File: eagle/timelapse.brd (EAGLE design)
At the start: 48.3 x 47 mm, 21 parts, among them Q1 200mA/40V, Q2 60V/32A/35mΩ, U2 TSR_1-2450

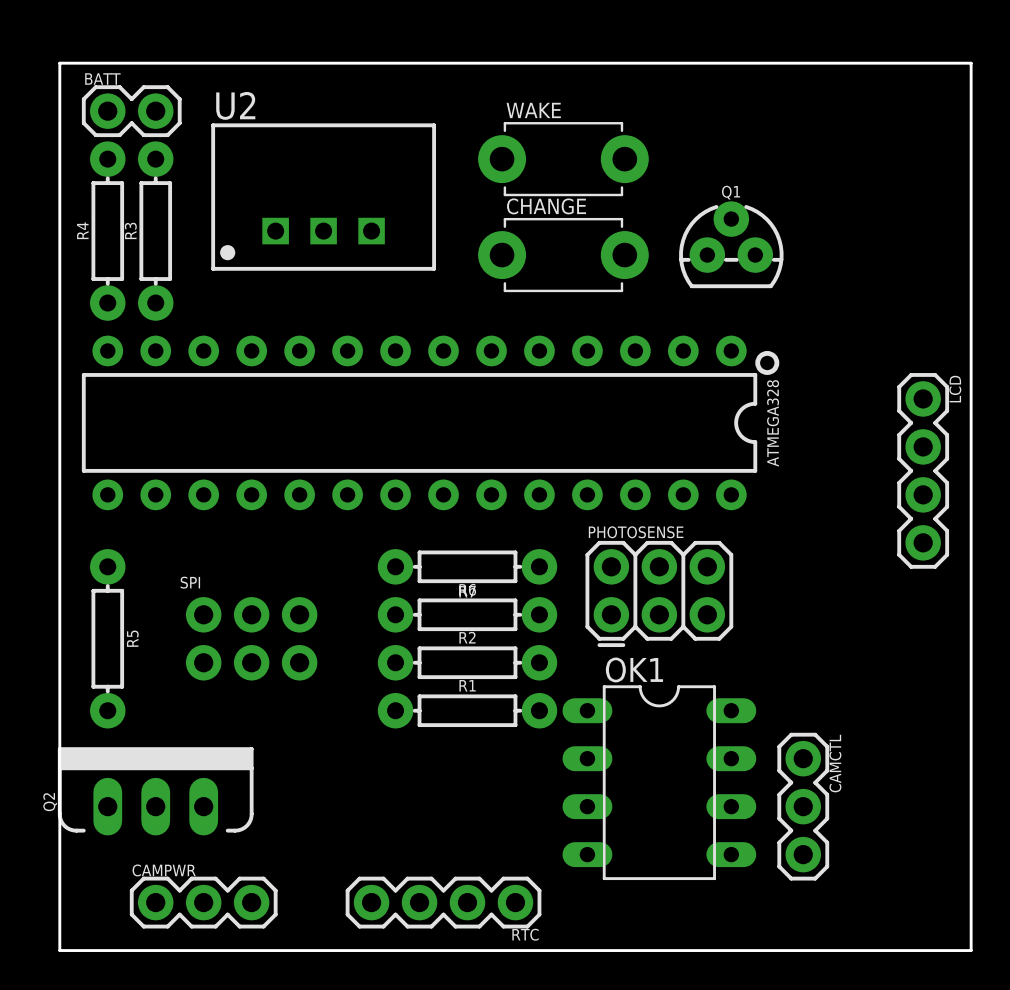
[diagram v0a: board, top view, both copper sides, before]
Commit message: Remove old EAGLE files, fix missing wires in schema and add test points.
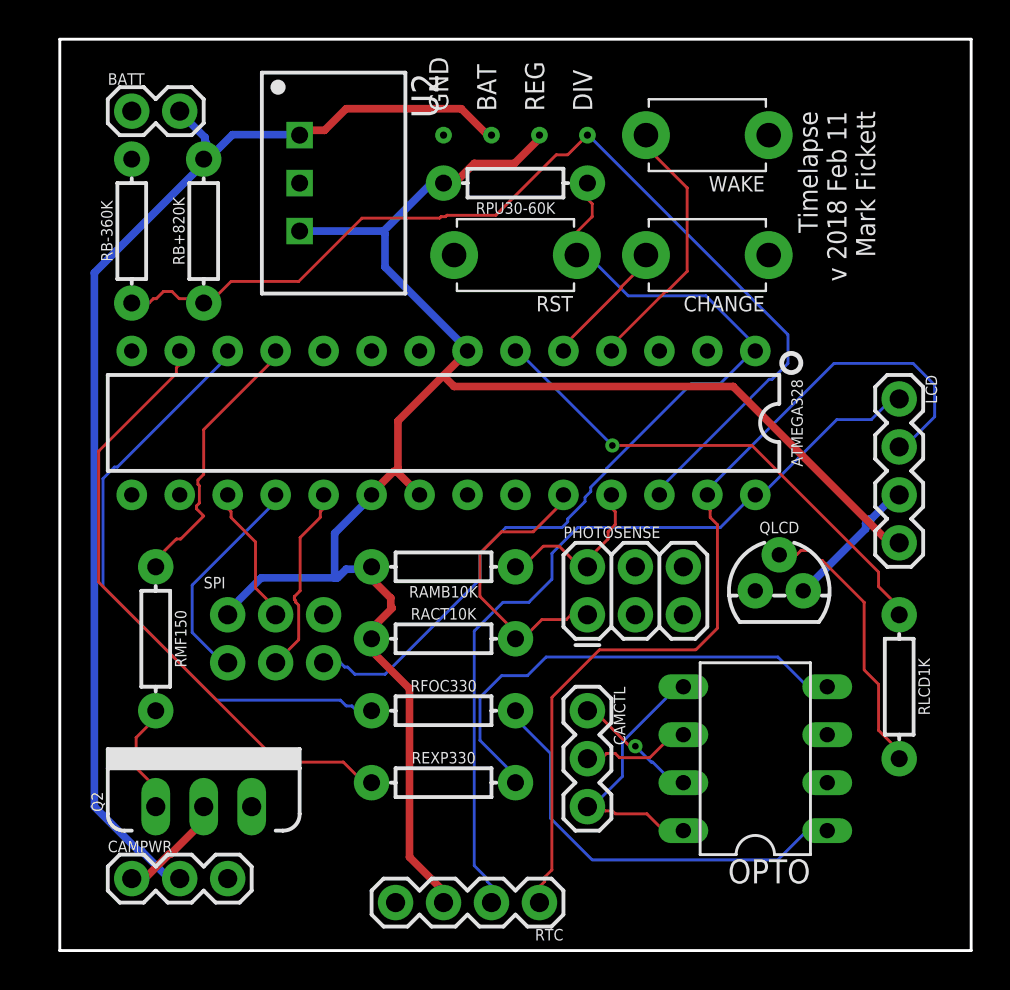
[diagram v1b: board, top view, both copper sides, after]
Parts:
- removed OK1: ILD2, optocoupler-2:DIL08
- removed Q1: 200mA/40V, SparkFun-DiscreteSemi:TO-92
- removed R1, R2, R5: 330, SparkFun-Resistors:AXIAL-0.3
- removed R3, R4, R6, R7: 10k, SparkFun-Resistors:AXIAL-0.3
- added OPTO: ILD2, optocoupler-2:DIL08
- added QLCD: 200mA/40V, SparkFun-DiscreteSemi:TO-92
- added RACT10K, RAMB10K: 10k, SparkFun-Resistors:AXIAL-0.3
- added RB+820K: 820k, SparkFun-Resistors:AXIAL-0.3
- added RB-360K: 360k, SparkFun-Resistors:AXIAL-0.3
- added REXP330, RFOC330: 330, SparkFun-Resistors:AXIAL-0.3
- added RLCD1K: 1k, SparkFun-Resistors:AXIAL-0.3
- added RMF150: 150, SparkFun-Resistors:AXIAL-0.3
- added RPU30-60K: 30-60k, SparkFun-Resistors:AXIAL-0.3
- added RST: (no value), adafruit:TACT_PANA-EVQ
- added TPBATT, TPDIV, TPGND, TPVREG: TEST-POINTTP_15TH_THRU, SparkFun-Connectors:TP_15TH
- moved CAMCTL 11.7 mm to (27.9, 12.7)
- moved WAKE 7.73 mm to (34.3, 43.2), turned to 180 degrees
- moved CHANGE 7.62 mm to (34.3, 36.8), turned to 180 degrees
- moved U2 2.84 mm to (12.7, 40.6), turned to 270 degrees
- moved Q2 2.54 mm to (7.62, 7.62)
- moved CAMPWR 1.80 mm to (3.81, 3.81)
- moved BATT 1.27 mm to (3.81, 44.5)
- moved ATMEGA328 1.27 mm to (20.3, 27.9)
- moved PHOTOSENSE 1.27 mm to (27.9, 17.8)
- moved RTC 1.27 mm to (25.4, 2.54)
- moved SPI 1.27 mm to (11.4, 16.5)
- moved LCD 1.27 mm to (44.5, 29.2)
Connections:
- removed net 3.3V: ATMEGA328.22, ATMEGA328.8, BATT.1, CHANGE.P$1, OK1.2, OK1.3, PHOTOSENSE.3, PHOTOSENSE.4, Q1.1, Q2.3, R4.P$2, RTC.4, SPI.6, U2.2, WAKE.P$1
- removed net N$4: ATMEGA328.12, R2.P$1
- removed net VCC2: BATT.2, CAMPWR.2, R3.P$2, U2.1
- new net BATVCC: BATT.2, CAMPWR.2, RB+820K.P$2, TPBATT.P$1, U2.1
- new net CAMGND: CAMCTL.3, OPTO.5, OPTO.8
- new net D6: ATMEGA328.12, RFOC330.P$1
- new net D7: ATMEGA328.13, REXP330.P$1
- new net RST: ATMEGA328.1, RPU30-60K.P$1, RST.P$1, SPI.5
- net ACTSENSE: now also RACT10K.P$2; no longer R6.P$2
- net AMBSENSE: now also RAMB10K.P$1; no longer R7.P$1
- net BATTSENSE: now also RB+820K.P$1, RB-360K.P$1, TPDIV.P$1; no longer R3.P$1, R4.P$1
- net D4: now also RLCD1K.P$1; no longer Q1.2
- net D5: now also RMF150.P$1; no longer R5.P$1
- net EXPOSE: now also OPTO.6; no longer OK1.6
- net FOCUS: now also OPTO.7; no longer OK1.7
- net GND: now also ATMEGA328.22, ATMEGA328.8, BATT.1, CHANGE.P$1, OPTO.2, OPTO.3, PHOTOSENSE.5, PHOTOSENSE.6, Q2.3, QLCD.1, RB-360K.P$2, RST.P$2, RTC.4, SPI.6, TPGND.P$1, U2.2, WAKE.P$1; no longer CAMCTL.3, OK1.5, OK1.8
- net N$1: now also OPTO.1, RFOC330.P$2; no longer OK1.1, R2.P$2
- net N$2: now also OPTO.4, REXP330.P$2; no longer OK1.4, R1.P$2
- net N$3: now also QLCD.2, RLCD1K.P$2; no longer ATMEGA328.13, R1.P$1
- net N$5: now also QLCD.3; no longer Q1.3
- net N$6: now also RMF150.P$2; no longer R5.P$2
- net VCCA: now also ATMEGA328.20, ATMEGA328.21, RACT10K.P$1, RAMB10K.P$2, RPU30-60K.P$2, TPVREG.P$1; no longer R6.P$1, R7.P$2
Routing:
- net VCCA: track 0.00 -> 96.7 mm
- net BATVCC: track 0.00 -> 63.0 mm
- net BATTSENSE: track 0.00 -> 54.7 mm
- net SDA: track 0.00 -> 48.5 mm
- net RST: track 0.00 -> 47.6 mm
- net SCL: track 0.00 -> 43.2 mm
- net D7: track 0.00 -> 32.9 mm
- net D6: track 0.00 -> 32.2 mm
- net D4: track 0.00 -> 26.8 mm, vias 0 -> 1
- net N$2: track 0.00 -> 25.2 mm
- net N$1: track 0.00 -> 22.7 mm
- net ACTSENSE: track 0.00 -> 15.8 mm
- net N$3: track 0.00 -> 14.8 mm
- net D5: track 0.00 -> 14.6 mm
- net CAMGND: track 0.00 -> 14.4 mm
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- added copper zone on layer 1, net GND
- added copper zone on layer 16, net GND
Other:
- board size 48.3 x 47 mm -> 48.3 x 48.3 mm
- board text added: "GND BAT REG DIV"
- board text added: "Timelapse v 2018 Feb 11 Mark Fickett"

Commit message: Add capacitor for camera power supply.
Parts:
- added C1: 22uF 50V, SparkFun-Capacitors:CPOL-RADIAL-2.5MM-5MM
- moved Q2 8.98 mm to (6.35, 16.5), turned to 270 degrees
- moved RMF150 2.54 mm to (2.54, 16.5)
- moved SPI 1.80 mm to (12.7, 17.8), turned to 270 degrees
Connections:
- net BATVCC: now also C1.1
- net GND: now also C1.2
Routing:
- net N$9: track 5.83 -> 16.3 mm
- net BATTSENSE: track 54.7 -> 47.2 mm
- net VCCA: track 96.7 -> 89.5 mm, vias 0 -> 1
- net MISO: track 11.7 -> 4.63 mm
- net D6: track 32.2 -> 25.9 mm
- net ACTSENSE: track 15.8 -> 11.0 mm
- net N$5: track 7.37 -> 12.1 mm
- net MOSI: track 7.40 -> 11.9 mm
- net BATVCC: track 63.0 -> 67.5 mm
- net N$2: track 25.2 -> 21.4 mm
- net SDA: track 48.5 -> 44.8 mm
- net RST: track 47.6 -> 51.0 mm, vias 0 -> 1
- net D5: track 14.6 -> 17.2 mm
- net SCK: track 10.1 -> 7.71 mm
- net N$6: track 5.97 -> 8.31 mm
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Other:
- board text added: "Timelapse v 2018 Feb 15 Mark Fickett"
- board text removed: "Timelapse v 2018 Feb 11 Mark Fickett"
